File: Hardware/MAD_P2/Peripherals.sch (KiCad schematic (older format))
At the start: 84 parts, among them J12 Micro_SD_Card, U28 DS3231M, U29 ESP-12F, U30 ADS131E08-REF

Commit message: finished board layout
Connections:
- net A1+: now also R39.1; no longer C119.2, R39.2
- net A1-: now also R40.1; no longer C120.1, R40.2
- net A2+: now also R41.1; no longer C121.2, R41.2
- net A2-: now also R42.1; no longer C122.1, R42.2
- net A3+: now also R43.1; no longer C123.2, R43.2
- net A3-: now also R44.1; no longer C124.1, R44.2
- net A4+: now also R45.1; no longer C125.2, R45.2
- net A4-: now also R46.1; no longer C126.1, R46.2
- net A5+: now also R47.1; no longer C127.2, R47.2
- net A5-: now also R48.1; no longer C128.1, R48.2
- net A6+: now also R49.1; no longer C129.2, R49.2
- net A6-: now also R50.1; no longer C130.1, R50.2
- net A7+: now also R51.1; no longer C131.2, R51.2
- net A7-: now also R52.1; no longer C132.1, R52.2
- net A8+: now also R53.1; no longer C133.2, R53.2
- net A8-: now also R54.1; no longer C134.1, R54.2
- net IN1N: now also C120.1, R40.2; no longer R40.1
- net IN1P: now also C119.2, R39.2; no longer R39.1
- net IN2N: now also C122.1, R42.2; no longer R42.1
- net IN2P: now also C121.2, R41.2; no longer R41.1
- net IN3N: now also C124.1, R44.2; no longer R44.1
- net IN3P: now also C123.2, R43.2; no longer R43.1
- net IN4N: now also C126.1, R46.2; no longer R46.1
- net IN4P: now also C125.2, R45.2; no longer R45.1
- net IN5N: now also C128.1, R48.2; no longer R48.1
- net IN5P: now also C127.2, R47.2; no longer R47.1
- net IN6N: now also C130.1, R50.2; no longer R50.1
- net IN6P: now also C129.2, R49.2; no longer R49.1
- net IN7N: now also C132.1, R52.2; no longer R52.1
- net IN7P: now also C131.2, R51.2; no longer R51.1
- net IN8N: now also C134.1, R54.2; no longer R54.1
- net IN8P: now also C133.2, R53.2; no longer R53.1
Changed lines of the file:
@@
 	1    0    0    -1
 $EndComp
-Text GLabel 8600 2100 0    50   Input ~ 0
+Text GLabel 9450 2100 2    50   Input ~ 0
 A1+
 Wire Wire Line
@@
 	-1   0    0    1
 $EndComp
-Text GLabel 8600 2350 0    50   Input ~ 0
+Text GLabel 9550 2350 2    50   Input ~ 0
 A1-
 $Comp
@@
 	1    0    0    -1
 $EndComp
-Text GLabel 8600 3200 0    50   Input ~ 0
+Text GLabel 9450 3200 2    50   Input ~ 0
 A2+
 Wire Wire Line
@@
 	-1   0    0    1
 $EndComp
-Text GLabel 8600 3450 0    50   Input ~ 0
+Text GLabel 9550 3450 2    50   Input ~ 0
 A2-
 $Comp
@@
 	1    0    0    -1
 $EndComp
-Text GLabel 8600 4300 0    50   Input ~ 0
+Text GLabel 9450 4300 2    50   Input ~ 0
 A3+
 Wire Wire Line
@@
 	-1   0    0    1
 $EndComp
-Text GLabel 8600 4550 0    50   Input ~ 0
+Text GLabel 9550 4550 2    50   Input ~ 0
 A3-
 $Comp
@@
 	1    0    0    -1
 $EndComp
-Text GLabel 8600 5400 0    50   Input ~ 0
+Text GLabel 9450 5400 2    50   Input ~ 0
 A4+
 Wire Wire Line
@@
 	-1   0    0    1
 $EndComp
-Text GLabel 8600 5650 0    50   Input ~ 0
+Text GLabel 9550 5650 2    50   Input ~ 0
 A4-
 $Comp
@@
 	1    0    0    -1
 $EndComp
-Text GLabel 10000 5400 0    50   Input ~ 0
+Text GLabel 10850 5400 2    50   Input ~ 0
 A8+
 Wire Wire Line
@@
 	-1   0    0    1
 $EndComp
-Text GLabel 10000 5650 0    50   Input ~ 0
+Text GLabel 10950 5650 2    50   Input ~ 0
 A8-
 $Comp
@@
 	1    0    0    -1
 $EndComp
-Text GLabel 10000 4300 0    50   Input ~ 0
+Text GLabel 10850 4300 2    50   Input ~ 0
 A7+
 Wire Wire Line
@@
 	-1   0    0    1
 $EndComp
-Text GLabel 10000 4550 0    50   Input ~ 0
+Text GLabel 10950 4550 2    50   Input ~ 0
 A7-
 $Comp
@@
 	1    0    0    -1
 $EndComp
-Text GLabel 10000 3200 0    50   Input ~ 0
+Text GLabel 10850 3200 2    50   Input ~ 0
 A6+
 Wire Wire Line
@@
 	-1   0    0    1
 $EndComp
-Text GLabel 10000 3450 0    50   Input ~ 0
+Text GLabel 10950 3450 2    50   Input ~ 0
 A6-
 $Comp
@@
 	1    0    0    -1
 $EndComp
-Text GLabel 10000 2100 0    50   Input ~ 0
+Text GLabel 10850 2100 2    50   Input ~ 0
 A5+
 Wire Wire Line
@@
 	-1   0    0    1
 $EndComp
-Text GLabel 10000 2350 0    50   Input ~ 0
+Text GLabel 10950 2350 2    50   Input ~ 0
 A5-
 Text Label 4950 4800 2    50   ~ 0
@@
 Text Label 4950 3300 2    50   ~ 0
 IN8N
-Text Label 9450 2100 0    50   ~ 0
+Text Label 8600 2100 2    50   ~ 0
 IN1P
-Text Label 9550 2350 0    50   ~ 0
+Text Label 8600 2350 2    50   ~ 0
 IN1N
-Text Label 9450 3200 0    50   ~ 0
+Text Label 8600 3200 2    50   ~ 0
 IN2P
-Text Label 9550 3450 0    50   ~ 0
+Text Label 8600 3450 2    50   ~ 0
 IN2N
-Text Label 9450 4300 0    50   ~ 0
+Text Label 8600 4300 2    50   ~ 0
 IN3P
-Text Label 9550 4550 0    50   ~ 0
+Text Label 8600 4550 2    50   ~ 0
 IN3N
-Text Label 9450 5400 0    50   ~ 0
+Text Label 8600 5400 2    50   ~ 0
 IN4P
-Text Label 9550 5650 0    50   ~ 0
+Text Label 8600 5650 2    50   ~ 0
 IN4N
-Text Label 10850 2100 0    50   ~ 0
+Text Label 10000 2100 2    50   ~ 0
 IN5P
-Text Label 10950 2350 0    50   ~ 0
+Text Label 10000 2350 2    50   ~ 0
 IN5N
-Text Label 10850 3200 0    50   ~ 0
+Text Label 10000 3200 2    50   ~ 0
 IN6P
-Text Label 10950 3450 0    50   ~ 0
+Text Label 10000 3450 2    50   ~ 0
 IN6N
-Text Label 10850 4300 0    50   ~ 0
+Text Label 10000 4300 2    50   ~ 0
 IN7P
-Text Label 10950 4550 0    50   ~ 0
+Text Label 10000 4550 2    50   ~ 0
 IN7N
-Text Label 10850 5400 0    50   ~ 0
+Text Label 10000 5400 2    50   ~ 0
 IN8P
-Text Label 10950 5650 0    50   ~ 0
+Text Label 10000 5650 2    50   ~ 0
 IN8N
 $Comp

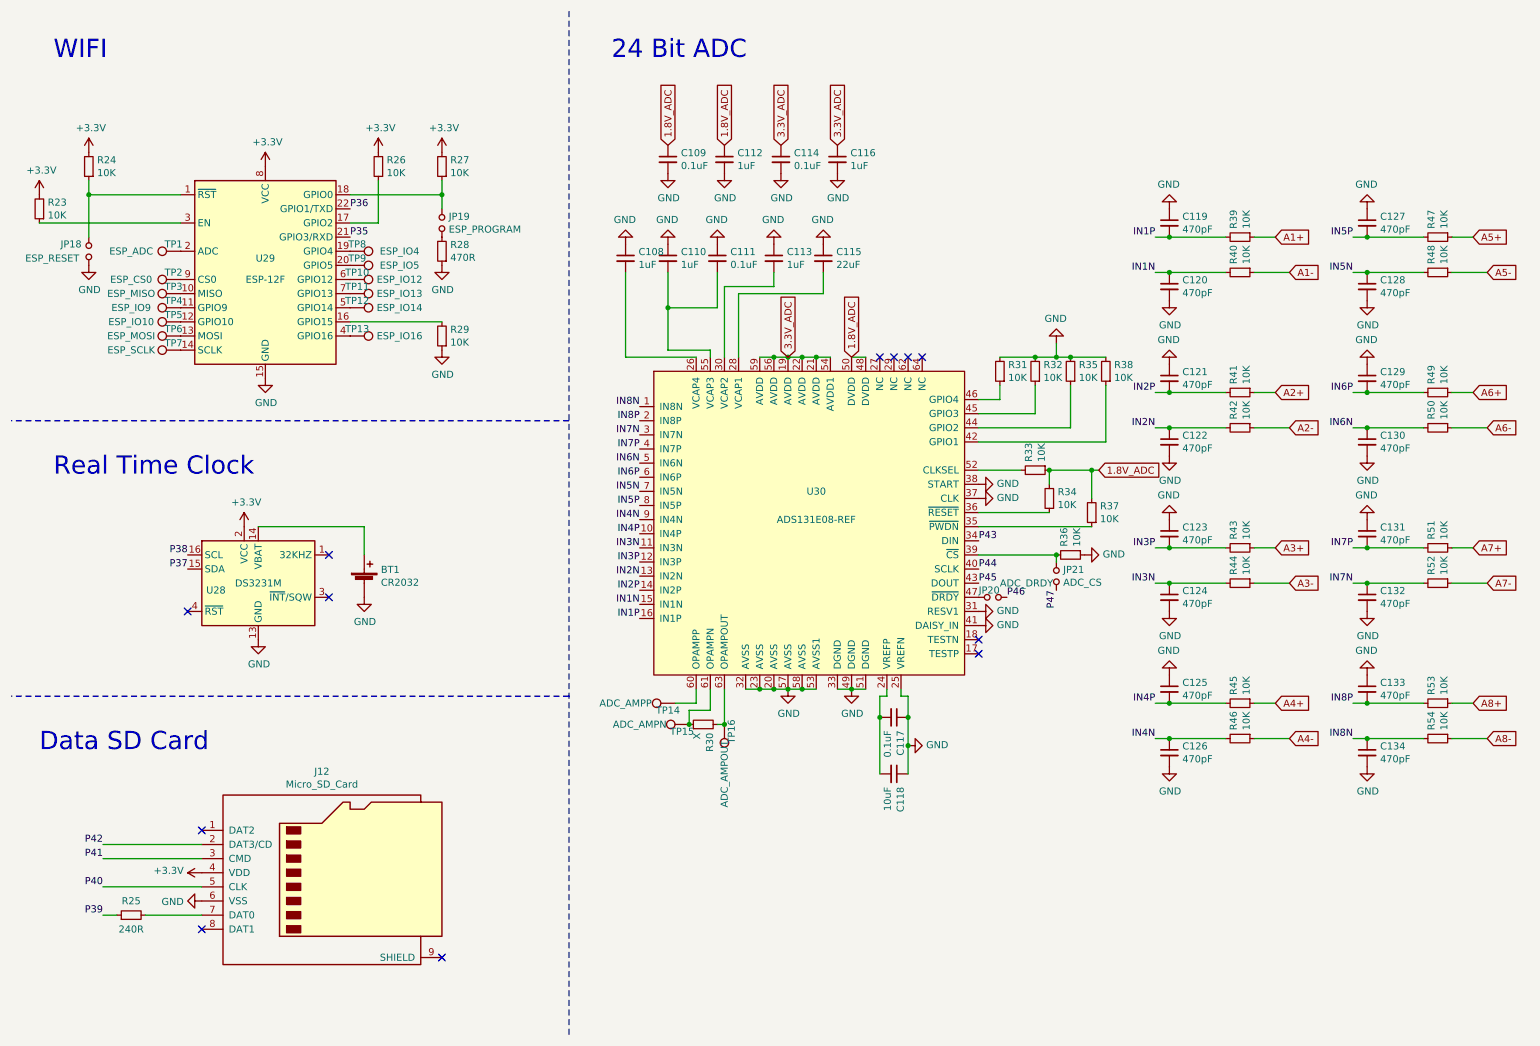
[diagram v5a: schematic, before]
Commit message: replaced ads131E with ads131A
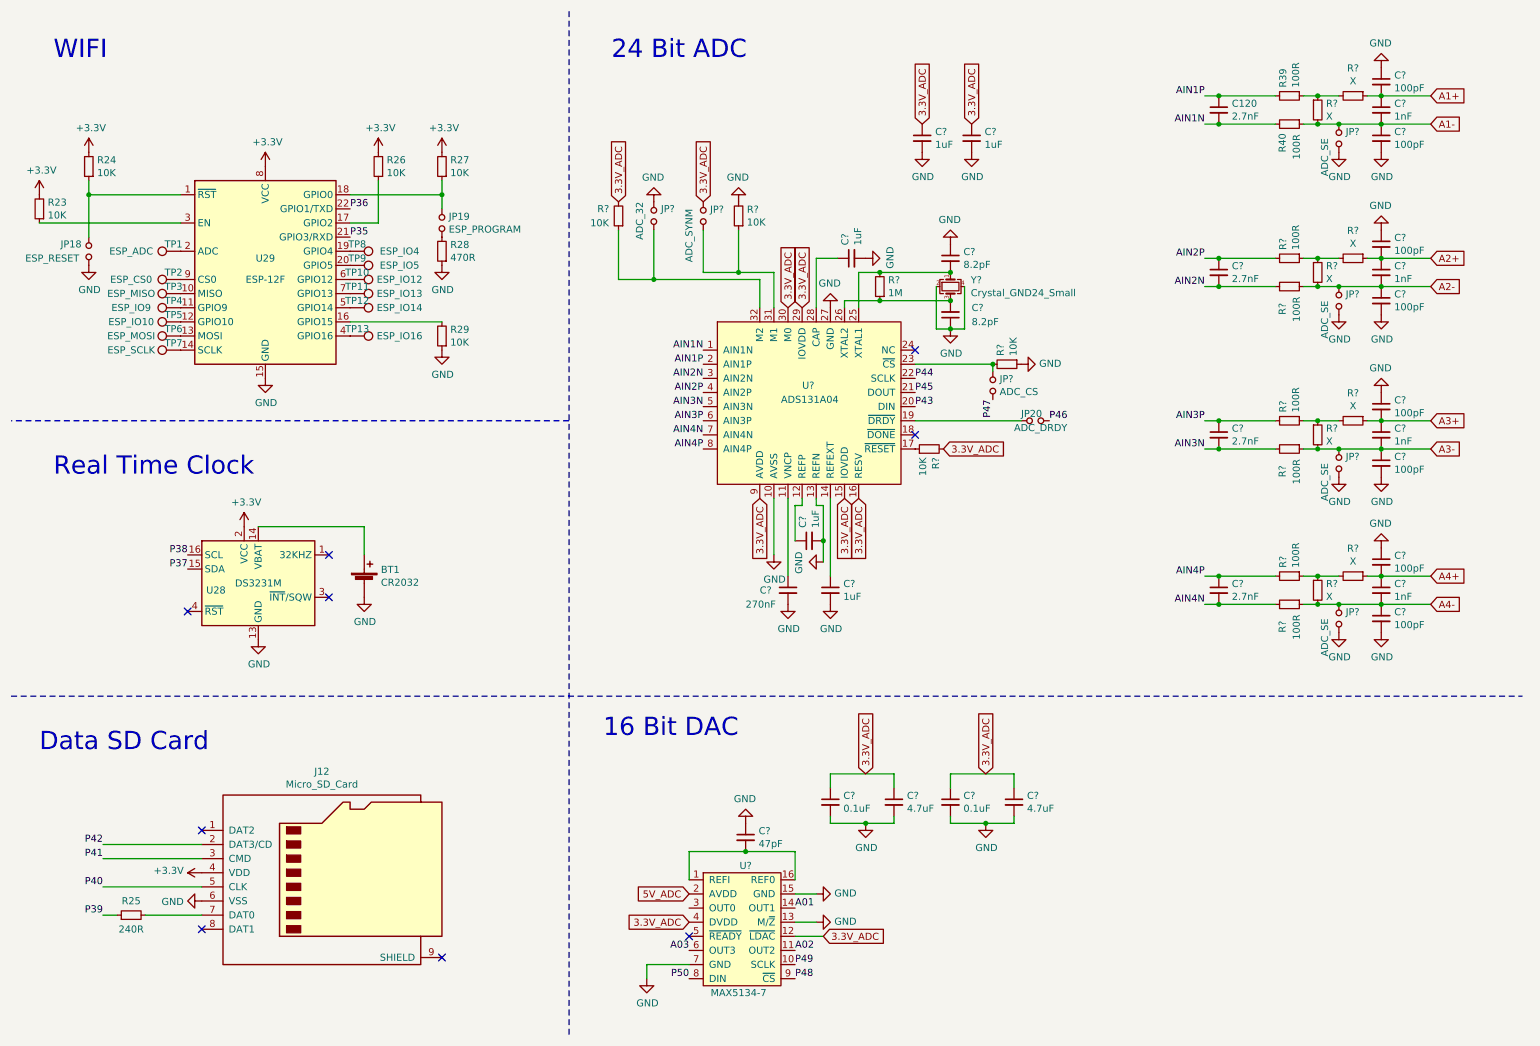
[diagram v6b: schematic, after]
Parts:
- removed C108, C110, C112, C113, C116: 1uF, Capacitor_SMD:C_0603_1608Metric, symbol Device:C_Small
- removed C109, C111, C114, C117: 0.1uF, Capacitor_SMD:C_0603_1608Metric, symbol Device:C_Small
- removed C115: 22uF, Capacitor_SMD:C_0603_1608Metric, symbol Device:C_Small
- removed C118: 10uF, Capacitor_SMD:C_0603_1608Metric, symbol Device:C_Small
- removed C119, C121, C122, C123, C124, C125, C126, C127, C128, C129, C130, C131, C132, C133, C134: 470pF, Capacitor_SMD:C_0603_1608Metric, symbol Device:C_Small
- removed JP21: ADC_CS, Jumper:SolderJumper-2_P1.3mm_Open_Pad1.0x1.5mm, symbol Device:Jumper_NO_Small
- removed R30: X, Resistor_SMD:R_0603_1608Metric, symbol Device:R_Small
- removed R31, R32, R33, R34, R35, R36, R37, R38, R41, R42, R43, R44, R45, R46, R47, R48, R49, R50, R51, R52, R53, R54: 10K, Resistor_SMD:R_0603_1608Metric, symbol Device:R_Small
- removed TP14: ADC_AMPP, TestPoint:TestPoint_Pad_1.0x1.0mm, symbol Connector:TestPoint
- removed TP15: ADC_AMPN, TestPoint:TestPoint_Pad_1.0x1.0mm, symbol Connector:TestPoint
- removed TP16: ADC_AMPOUT, TestPoint:TestPoint_Pad_1.0x1.0mm, symbol Connector:TestPoint
- removed U30: ADS131E08-REF, Package_QFP:TQFP-64_10x10mm_P0.5mm, symbol MAD_P2-rescue:ADS131E08-REF
- added C? (x5): 1uF, Capacitor_SMD:C_0603_1608Metric, symbol Device:C_Small
- added C?: 270nF, symbol Device:C_Small
- added C? (x2): 8.2pF, symbol Device:C_Small
- added C? (x4): 1nF, Capacitor_SMD:C_0603_1608Metric, symbol Device:C_Small
- added C? (x8): 100pF, Capacitor_SMD:C_0603_1608Metric, symbol Device:C_Small
- added C? (x3): 2.7nF, Capacitor_SMD:C_0603_1608Metric, symbol Device:C_Small
- added C?: 47pF, Capacitor_SMD:C_0603_1608Metric, symbol Device:C_Small
- added C? (x2): 0.1uF, Capacitor_SMD:C_0603_1608Metric, symbol Device:C_Small
- added C? (x2): 4.7uF, Capacitor_SMD:C_0603_1608Metric, symbol Device:C_Small
- added JP?: ADC_CS, Jumper:SolderJumper-2_P1.3mm_Open_Pad1.0x1.5mm, symbol Device:Jumper_NO_Small
- added JP?: ADC_SYNM, Jumper:SolderJumper-2_P1.3mm_Open_Pad1.0x1.5mm, symbol Device:Jumper_NO_Small
- added JP?: ADC_32, Jumper:SolderJumper-2_P1.3mm_Open_Pad1.0x1.5mm, symbol Device:Jumper_NO_Small
- added JP? (x4): ADC_SE, Jumper:SolderJumper-2_P1.3mm_Open_Pad1.0x1.5mm, symbol Device:Jumper_NO_Small
- added R? (x4): 10K, Resistor_SMD:R_0603_1608Metric, symbol Device:R_Small
- added R?: 1M, symbol Device:R_Small
- added R? (x8): X, symbol Device:R_Small
- added R? (x6): 100R, Resistor_SMD:R_0603_1608Metric, symbol Device:R_Small
- added U?: ADS131A04, symbol MAD_P2-rescue:ADS131A04
- added U?: MAX5134-7, Package_SO:TSSOP-16_4.4x5mm_P0.65mm, symbol MAD_P2-rescue:MAX5134-7
- added Y?: Crystal_GND24_Small, symbol Device:Crystal_GND24_Small
- C120: value 470pF -> 2.7nF
- R39, R40: value 10K -> 100R
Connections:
- net 3.3V_ADC: now also C?.1, C?.1, C?.1, C?.1, C?.1, C?.1, JP?.1, R?.2, R?.2, U?.12 (~LDAC), U?.15 (IOVDD), U?.16 (RESV), U?.29 (IOVDD), U?.30 (M0), U?.4 (DVDD), U?.9 (AVDD)
- net A1+: now also C?.1, C?.2, R?.1; no longer R39.1
- net A1-: now also C?.1, C?.2, JP?.1, R?.2
- net A2+: now also C?.1, C?.2, R?.1
- net A2-: now also C?.1, C?.2, JP?.1, R?.1, R?.2
- net A3+: now also C?.1, C?.2, R?.1
- net A3-: now also C?.1, C?.2, JP?.1, R?.1, R?.2
- net A4+: now also C?.1, C?.2, R?.1
- net A4-: now also C?.1, C?.2, JP?.1, R?.1, R?.2
- net GND: now also C?.1, C?.1, C?.1, C?.1, C?.1, C?.1, C?.1, C?.2, C?.2, C?.2, C?.2, C?.2, C?.2, C?.2, C?.2, C?.2, C?.2, C?.2, C?.2, C?.2, C?.2, JP?.1, JP?.2, JP?.2, JP?.2, JP?.2, R?.1, R?.2, U?.10 (AVSS), U?.13 (M/~Z), U?.13 (REFN), U?.15 (GND), U?.27 (GND), U?.7 (GND), Y?.2, Y?.4; no longer C120.2
- net P43: now also U?.20 (DIN)
- net P44: now also U?.22 (SCLK)
- net P45: now also U?.21 (DOUT)
- net P47: now also JP?.2
- net at JP20.1: now also U?.19 (~DRDY)
- net IN1N renamed AIN1N
- net AIN1N: now also C120.2, U?.1 (AIN1N); no longer C120.1
- net IN1P renamed AIN1P
- net AIN1P: now also C120.1, U?.2 (AIN1P)
- new net: C?.1, U?.11 (VNCP)
- new net: C?.1, U?.12 (REFP)
- new net: C?.1, U?.14 (REFEXT)
- new net: R?.1, U?.17 (~RESET)
- new net: JP?.1, R?.2, U?.23 (~CS)
- new net: C?.2, R?.2, U?.25 (XTAL1), Y?.1
- new net: C?.2, R?.1, U?.26 (XTAL2), Y?.3
- new net: C?.1, U?.28 (CAP)
- new net: JP?.2, R?.1, U?.31 (M1)
- new net: JP?.2, R?.1, U?.32 (M2)
- new net: R39.1, R?.1, R?.2
- new net: R?.1, R?.1, R?.2 (x3)
- new net: C?.2, U?.1 (REFI), U?.16 (REF0)
- new net 5V_ADC: U?.2 (AVDD)
- new net A01: U?.14 (OUT1)
- new net A02: U?.11 (OUT2)
- new net A03: U?.6 (OUT3)
- new net AIN2N: C?.2, R?.2, U?.3 (AIN2N)
- new net AIN2P: C?.1, R?.2, U?.4 (AIN2P)
- new net AIN3N: C?.2, R?.2, U?.5 (AIN3N)
- new net AIN3P: C?.1, R?.2, U?.6 (AIN3P)
- new net AIN4N: C?.2, R?.2, U?.7 (AIN4N)
- new net AIN4P: C?.1, R?.2, U?.8 (AIN4P)
- new net P48: U?.9 (~CS)
- new net P49: U?.10 (SCLK)
- new net P50: U?.8 (DIN)
- no-connect marks 12 -> 9
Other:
- note added: "16 Bit DAC"
- moved on the sheet: C120, JP20, R39, R40
